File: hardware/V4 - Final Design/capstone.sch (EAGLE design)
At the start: 32 parts, among them J1 61300311121, J2 61300311121, J3 61300311121, U1 BMP388, U2 LSM9DS1TR, U3 RFM95W-915S2

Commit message: Schematic Cleanup
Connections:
- net +3V3: now also C3.1; no longer C3.2
- net GND: now also C3.2; no longer C3.1
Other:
- note added: "3.3V"
- note added: "Accel/Gyro Data Enable"
- note added: "Accel/Gyro/Mag Data Ready Interrupt"
- note added: "Analog I/O"
- note added: "BMP-388 Barometer"
- note added: "Backup Voltage CR1220 Coin Cell"
- note added: "Barometer"
- note added: "Battery"
- note added: "Block Diagram"
- note added: "Ceramic Capacitors"
- note added: "Chip is in I2C mode if both CS pins are pulled high CS_M and CS_A/G"
- note added: "Controller"
- note added: "Digital I/O"
- note added: "GPS"
- note added: "I2C Bus"
- note added: "IMU"
- note added: "In I2C mode, SCL to SCK and SDA to SDI. Interrupt pin can be used to check for new data."
- note added: "LEDs"
- note added: "LSM9DS1 9-DOF IMU"
- note added: "MTK3339 GPS Module"
- note added: "No Fix: LED pulse up and down every second Fix: LED pulse every 15 seconds"
- note added: "Onboard Regulator"
- note added: "RFM95W Radio"
- note added: "Radio"
- note added: "SDO_A/G LSB for A/G I2C Address Pulled low - 0x6A"
- note added: "SDO_M LSB for Mag I2C Address Pulled low - 0x1C"
- note added: "SPI Bus"
- note added: "Servos - Rudder - Left Elevon - Right Elevon"
- note added: "Teensy 3.2 has a built-in voltage regulator"
- note added: "UART"
- note added: "Voltage Input"
- note removed: "AG Data Enable"
- note removed: "BMP-388"
- note removed: "Ceramic Capacitor"
- note removed: "Could put a pull up and diode on RX to ensure 3.3V but Teensy3.2 is 3.3V"
- note removed: "If CS pins are pulled high, use I2C mode"
- note removed: "In Two Wire I2C mode, SCL to SCK and SDA to SDI. Interrupt pin can be used to check for new data."
- note removed: "No fix, LED pulse up and down every second Fix, LED pulse every 15 seconds"
- note removed: "SDO_A/G LSB for A/G I2C Address Pulled low - 0x6a"
- note removed: "SDO_M LSB for Mag I2C Address Pulled low - 0x1c"
- moved on the sheet: ANT1, C1, C2, C3, C4, C7, C8, C9, FIX_LED, G1, R10

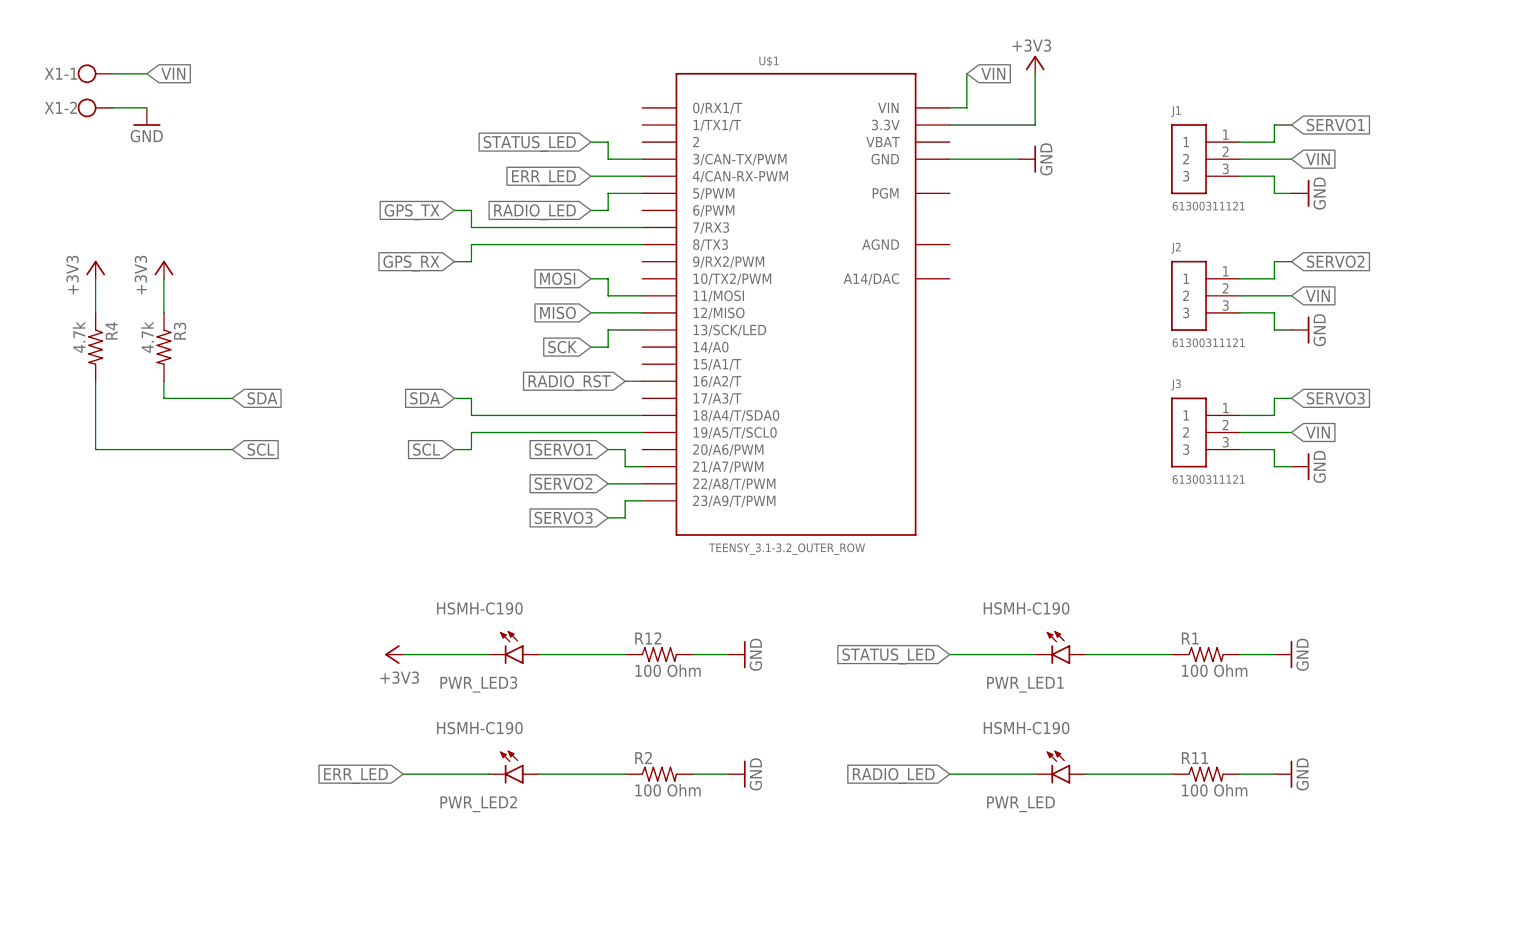
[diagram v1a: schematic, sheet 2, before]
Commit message: add test points to final design
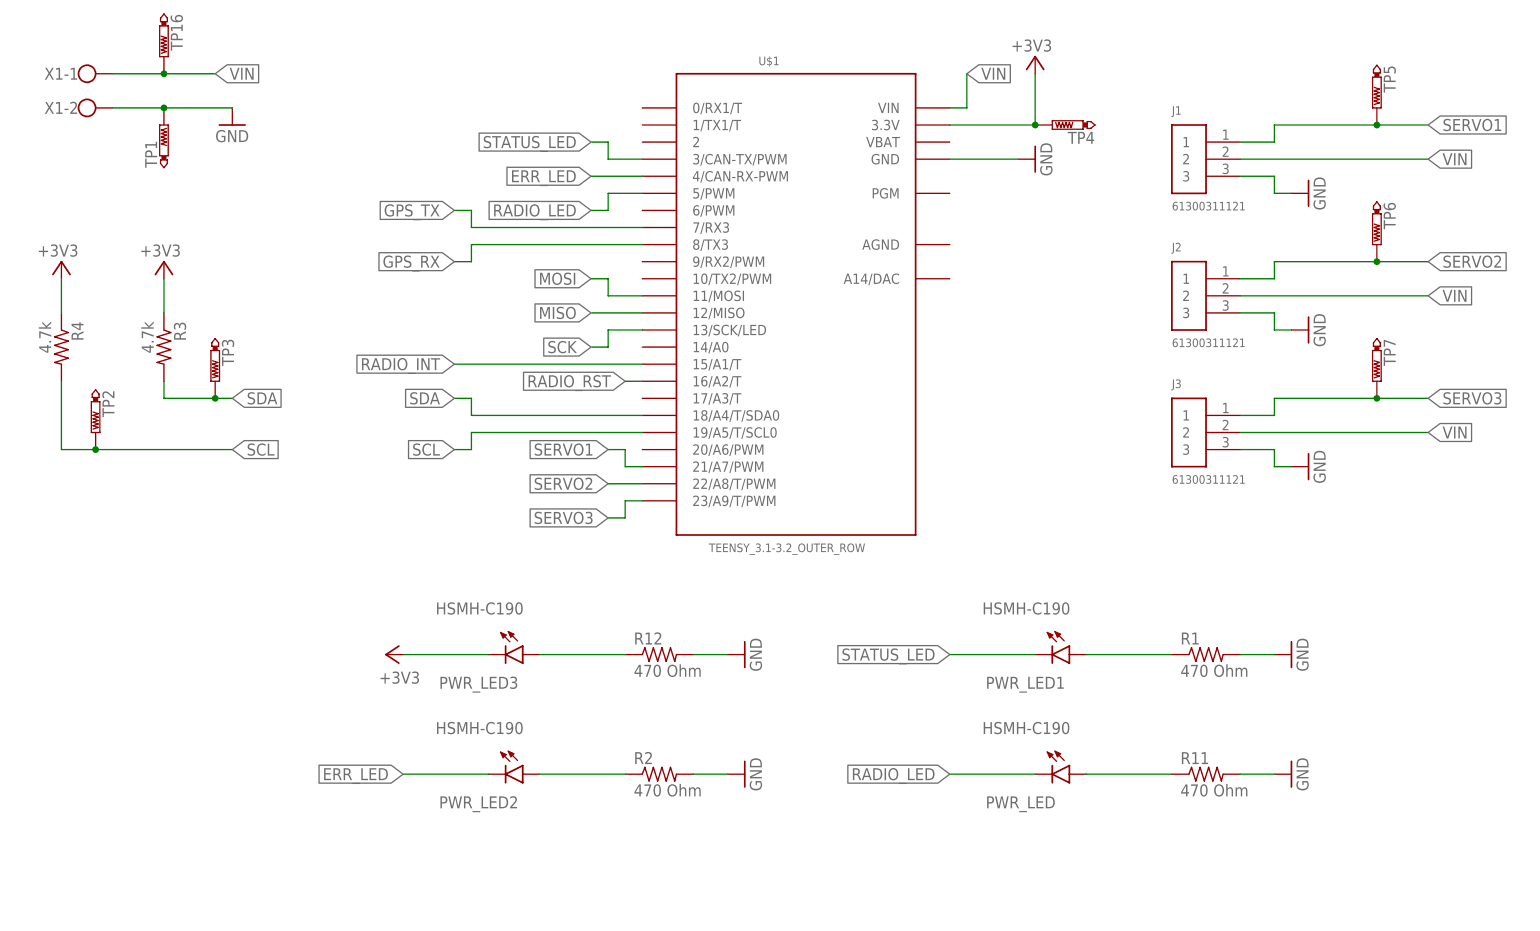
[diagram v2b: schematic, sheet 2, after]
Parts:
- added TP1, TP10, TP11, TP12, TP13, TP14, TP15, TP16, TP17, TP18, TP2, TP3, TP4, TP5, TP6, TP7, TP8, TP9: PTR1PAD1-20, testpad:PTR1PAD1-20
- R1, R11, R12, R2: value 100 Ohm -> 470 Ohm
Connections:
- net +3V3: now also TP10.TP, TP17.TP, TP4.TP, TP8.TP, TP9.TP
- net GND: now also TP1.TP
- net MISO: now also TP12.TP
- net MOSI: now also TP18.TP
- net RADIO_INT: now also TP15.TP, U$1.15/A1/T
- net RADIO_RST: now also TP14.TP
- net SCK: now also TP13.TP
- net SCL: now also TP2.TP
- net SDA: now also TP3.TP
- net SERVO1: now also TP5.TP
- net SERVO2: now also TP6.TP
- net SERVO3: now also TP7.TP
- net VBACKUP: now also TP11.TP
- net VIN: now also TP16.TP
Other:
- moved on the sheet: C4, R4

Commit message: finalized board design for final design
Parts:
- added H1, H2, H3, H4: MOUNT-HOLE2.8, holes:MOUNT-HOLE2.8
- C1, C4: value 10 uF -> 10 u
- C2: value 100 nF -> 100 n
- C3: value 0.1 uF -> 0.1u
- TP1, TP10, TP11, TP12, TP13, TP14, TP15, TP16, TP17, TP18, TP2, TP3, TP4, TP5, TP6, TP7, TP8, TP9: value PTR1PAD1-20 -> PTR1B1,27; device testpad:PTR1PAD1-20 -> testpad:PTR1B1,27
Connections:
- net +3V3: now also TP11.TP; no longer TP10.TP
- net GND: now also TP16.TP; no longer TP1.TP
- net VBACKUP: now also TP10.TP; no longer TP11.TP
- net VIN: now also TP1.TP; no longer TP16.TP
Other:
- moved on the sheet: TP1, TP10, TP11, TP13, TP14, TP15, TP16, TP17, TP2, TP5, TP6, TP7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

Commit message: design update for hardware
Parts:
- removed PWR_LED, PWR_LED1, PWR_LED2, PWR_LED3: HSMH-C190, LED:HSMH-C190
- added LED1, LED2, LED3, LED4: HSMH-C190, LED:HSMH-C190
- C1, C4: value 10 u -> 10u
- C2: value 100 n -> 100n
- C3: value 0.1u -> 100n
- C7, C8: value 100 nF -> 100n
- C9: value 10 nF -> 10n
- R1, R11, R12, R2: value 470 Ohm -> 82
- renumbered FIX_LED to LED5
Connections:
- removed net N$8: PWR_LED2.A, R2.1
- new net N$6: LED1.C, R12.1
- net +3V3: now also LED1.A; no longer PWR_LED3.C
- net ERR_LED: now also LED2.A; no longer PWR_LED2.C
- net N$10: now also LED3.C, R1.1; no longer PWR_LED.A, R11.1
- net N$7: now also LED2.C, R2.1; no longer PWR_LED3.A, R12.1
- net N$9: now also LED4.C, R11.1; no longer PWR_LED1.A, R1.1
- net RADIO_LED: now also LED4.A; no longer PWR_LED.C
- net STATUS_LED: now also LED3.A; no longer PWR_LED1.C
